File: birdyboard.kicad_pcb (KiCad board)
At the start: 2 copper layers, 18 parts, among them J1 24V Input Screw Terminal, J10 JST-PH StepMotor Conn, J11 TBP02R2-381-04BE, J2 24V Input Screw Terminal, J3 24V Input Screw Terminal, J4 JST-PH StepMotor Conn, J5 JST-PH StepMotor Conn, J6 JST-PH StepMotor Conn, J7 TBP02R2-381-04BE, J8 TBP02R2-381-04BE, J9 TBP02R2-381-04BE, U1 TMC2208_SILENTSTEPSTICK, U2 TMC2208_SILENTSTEPSTICK, U3 Pico, U4 TMC2208_SILENTSTEPSTICK, U5 TMC2208_SILENTSTEPSTICK, U7 AZ1117CH-3_3TRG1

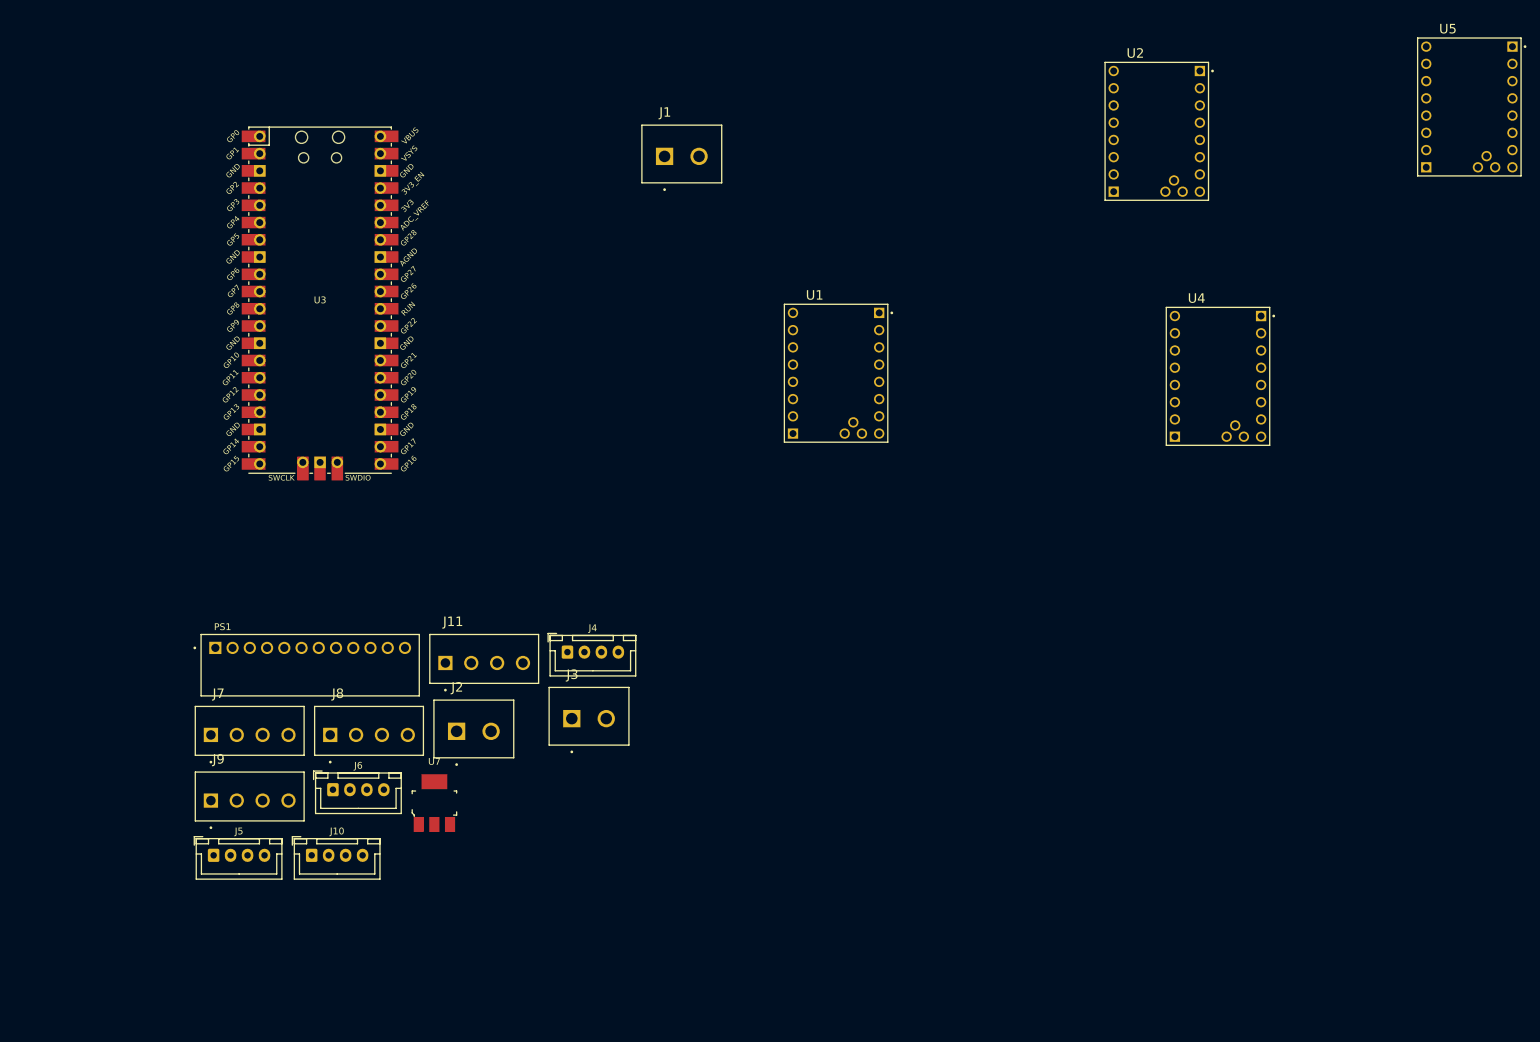
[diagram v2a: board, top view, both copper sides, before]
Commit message: Fixes most footprints and places footprints roughly at their final resting place
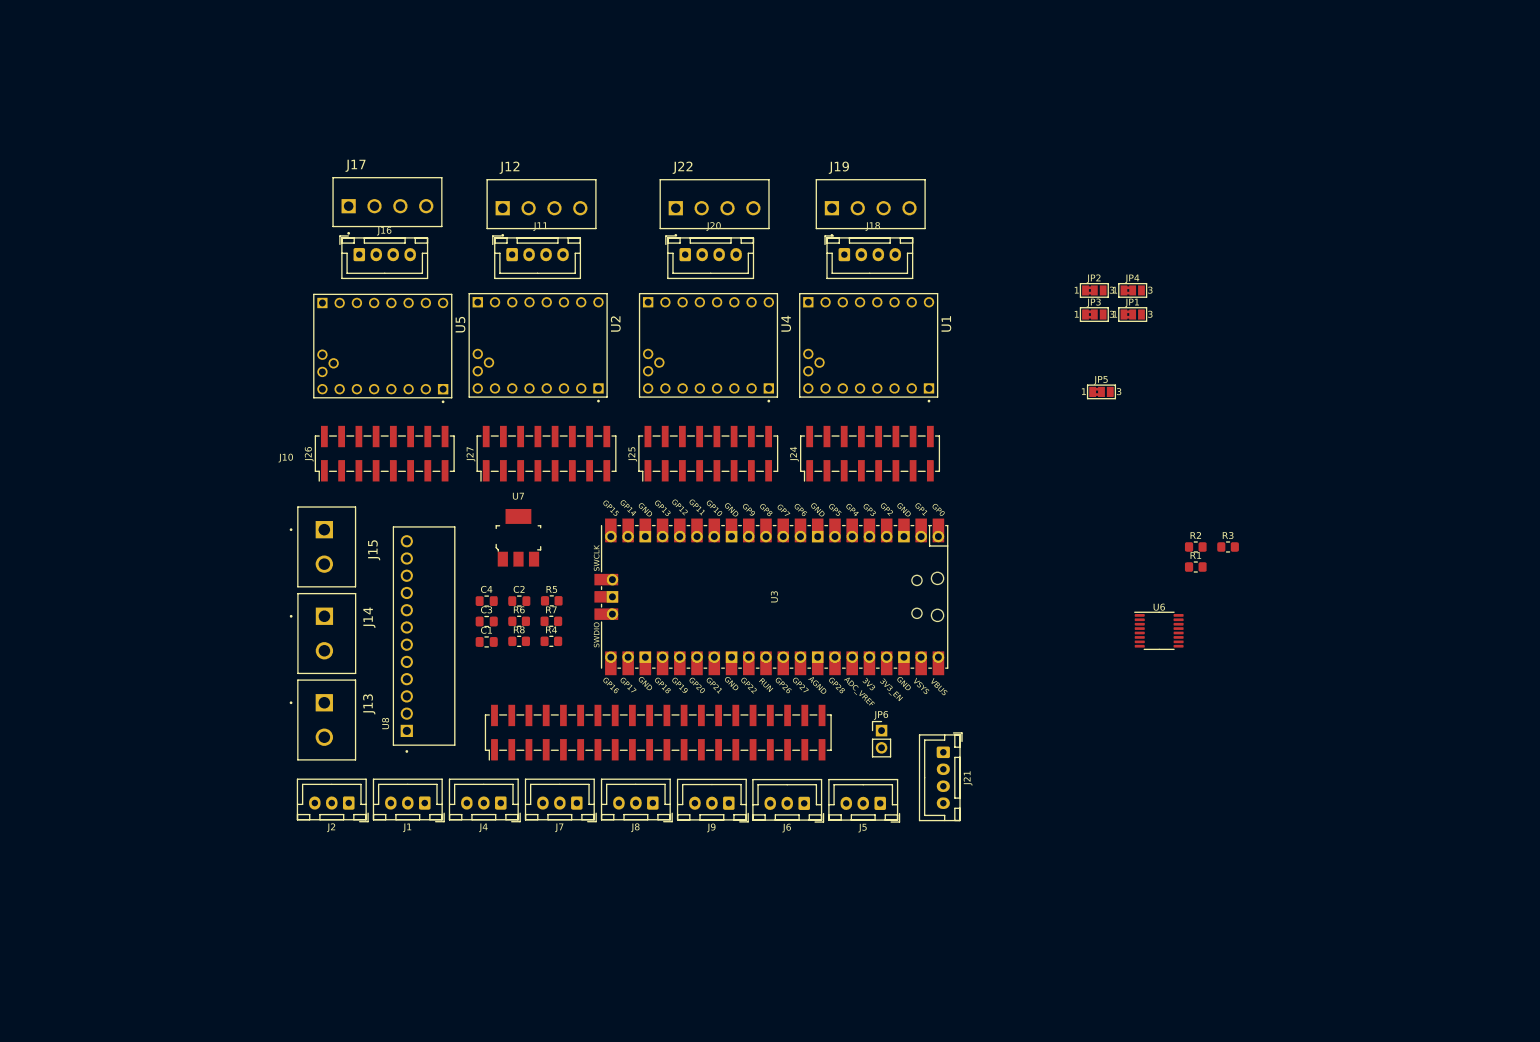
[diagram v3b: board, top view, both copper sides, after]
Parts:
- removed J3: 24V Input Screw Terminal, birdyboard:CUI_TBP01R2-508-02BE
- removed PS1: K7805-3AR3, birdyboard:CONV_K7805-3AR3
- added C1: 10uF 50V, Capacitor_SMD:C_0805_2012Metric_Pad1.18x1.45mm_HandSolder, F.Cu at (101.3, 118.4)
- added C2: 10uF 10V, Capacitor_SMD:C_0805_2012Metric_Pad1.18x1.45mm_HandSolder, F.Cu at (106.1, 112.4)
- added C3: 22uF 10V, Capacitor_SMD:C_0805_2012Metric_Pad1.18x1.45mm_HandSolder, F.Cu at (101.3, 115.4)
- added C4: 22uF 10V, Capacitor_SMD:C_0805_2012Metric_Pad1.18x1.45mm_HandSolder, F.Cu at (101.3, 112.4)
- added J12: TBP02R2-381-04BE, birdyboard:CUI_TBP02R2-381-04BE, F.Cu at (103.7, 54.5)
- added J13: Screw_Terminal_01x02, birdyboard:CUI_TBP01R2-508-02BE, F.Cu at (77.4, 127.4)
- added J14: Screw_Terminal_01x02, birdyboard:CUI_TBP01R2-508-02BE, F.Cu at (77.4, 114.7)
- added J15: Screw_Terminal_01x02, birdyboard:CUI_TBP01R2-508-02BE, F.Cu at (77.4, 101.9)
- added J16: JST-PH StepMotor Conn, Connector_JST:JST_XH_B4B-XH-A_1x04_P2.50mm_Vertical, F.Cu at (82.5, 61.4)
- added J17: TBP02R2-381-04BE, birdyboard:CUI_TBP02R2-381-04BE, F.Cu at (81.0, 54.2)
- added J18: JST-PH StepMotor Conn, Connector_JST:JST_XH_B4B-XH-A_1x04_P2.50mm_Vertical, F.Cu at (154.0, 61.4)
- added J19: TBP02R2-381-04BE, birdyboard:CUI_TBP02R2-381-04BE, F.Cu at (152.2, 54.5)
- added J20: JST-PH StepMotor Conn, Connector_JST:JST_XH_B4B-XH-A_1x04_P2.50mm_Vertical, F.Cu at (130.6, 61.4)
- added J21: JST-PH UART Conn, Connector_JST:JST_XH_B4B-XH-A_1x04_P2.50mm_Vertical, F.Cu at (168.6, 134.7)
- added J22: TBP02R2-381-04BE, birdyboard:CUI_TBP02R2-381-04BE, F.Cu at (129.2, 54.5)
- added J24: AS5047_Adapter_Board_Connector, Connector_PinHeader_2.54mm:PinHeader_2x08_P2.54mm_Vertical_SMD, F.Cu at (157.8, 90.7)
- added J25: AS5047_Adapter_Board_Connector, Connector_PinHeader_2.54mm:PinHeader_2x08_P2.54mm_Vertical_SMD, F.Cu at (134.0, 90.7)
- added J26: AS5047_Adapter_Board_Connector, Connector_PinHeader_2.54mm:PinHeader_2x08_P2.54mm_Vertical_SMD, F.Cu at (86.3, 90.7)
- added J27: AS5047_Adapter_Board_Connector, Connector_PinHeader_2.54mm:PinHeader_2x08_P2.54mm_Vertical_SMD, F.Cu at (110.1, 90.7)
- added JP1: SolderJumper_3_Bridged12, Jumper:SolderJumper-3_P1.3mm_Bridged2Bar12_Pad1.0x1.5mm_NumberLabels, F.Cu at (196.5, 70.2)
- added JP2: SolderJumper_3_Bridged12, Jumper:SolderJumper-3_P1.3mm_Bridged2Bar12_Pad1.0x1.5mm_NumberLabels, F.Cu at (190.8, 66.7)
- added JP3: SolderJumper_3_Bridged12, Jumper:SolderJumper-3_P1.3mm_Bridged2Bar12_Pad1.0x1.5mm_NumberLabels, F.Cu at (190.8, 70.2)
- added JP4: SolderJumper_3_Bridged12, Jumper:SolderJumper-3_P1.3mm_Bridged2Bar12_Pad1.0x1.5mm_NumberLabels, F.Cu at (196.5, 66.7)
- added JP5: Jumper_3_Open, Jumper:SolderJumper-3_P1.3mm_Bridged2Bar12_Pad1.0x1.5mm_NumberLabels, F.Cu at (191.9, 81.6)
- added JP6: Jumper_2_Open, Connector_PinHeader_2.54mm:PinHeader_1x02_P2.54mm_Vertical, F.Cu at (159.5, 131.5)
- added R1: R, Resistor_SMD:R_0805_2012Metric_Pad1.20x1.40mm_HandSolder, F.Cu at (205.8, 107.4)
- added R2: R, Resistor_SMD:R_0805_2012Metric_Pad1.20x1.40mm_HandSolder, F.Cu at (205.8, 104.5)
- added R3: R, Resistor_SMD:R_0805_2012Metric_Pad1.20x1.40mm_HandSolder, F.Cu at (210.6, 104.5)
- added R4: R, Resistor_SMD:R_0805_2012Metric_Pad1.20x1.40mm_HandSolder, F.Cu at (110.8, 118.3)
- added R5: R, Resistor_SMD:R_0805_2012Metric_Pad1.20x1.40mm_HandSolder, F.Cu at (110.9, 112.4)
- added R6: R, Resistor_SMD:R_0805_2012Metric_Pad1.20x1.40mm_HandSolder, F.Cu at (106.1, 115.4)
- added R7: R, Resistor_SMD:R_0805_2012Metric_Pad1.20x1.40mm_HandSolder, F.Cu at (110.8, 115.4)
- added R8: R, Resistor_SMD:R_0805_2012Metric_Pad1.20x1.40mm_HandSolder, F.Cu at (106.1, 118.3)
- added U6: SN74CBT3253 MUX/DEMUX, Package_SO:TSSOP-16_4.4x5mm_P0.65mm, F.Cu at (200.4, 116.8)
- added U8: K7805-3AR3, birdyboard:CONV_K7805-3AR3, F.Cu at (92.1, 117.6)
- J1, J2: value 24V Input Screw Terminal -> JST_3pin; footprint birdyboard:CUI_TBP01R2-508-02BE -> Connector_JST:JST_XH_B3B-XH-A_1x03_P2.50mm_Vertical
- J10: value JST-PH StepMotor Conn -> Conn_02x20_Odd_Even; footprint Connector_JST:JST_XH_B4B-XH-A_1x04_P2.50mm_Vertical -> Connector_PinHeader_2.54mm:PinHeader_2x20_P2.54mm_Vertical_SMD
- J11: value TBP02R2-381-04BE -> JST-PH StepMotor Conn; footprint birdyboard:CUI_TBP02R2-381-04BE -> Connector_JST:JST_XH_B4B-XH-A_1x04_P2.50mm_Vertical
- J4, J5, J6: value JST-PH StepMotor Conn -> JST_3pin; footprint Connector_JST:JST_XH_B4B-XH-A_1x04_P2.50mm_Vertical -> Connector_JST:JST_XH_B3B-XH-A_1x03_P2.50mm_Vertical
- J7, J8, J9: value TBP02R2-381-04BE -> JST_3pin; footprint birdyboard:CUI_TBP02R2-381-04BE -> Connector_JST:JST_XH_B3B-XH-A_1x03_P2.50mm_Vertical
- U1, U2, U4, U5: value TMC2208_SILENTSTEPSTICK -> TMC2209_SILENTSTEPSTICK
- moved U5 163.9 mm to (86.0, 74.8), turned to -90 degrees
- moved J1 101.6 mm to (92.2, 142.2), turned to 180 degrees
- moved J5 98.5 mm to (159.3, 142.2), turned to 180 degrees
- moved U2 96.5 mm to (108.9, 74.7), turned to -90 degrees
- moved U3 80.0 mm to (143.7, 111.8), turned to -90 degrees
- moved J9 76.3 mm to (137.0, 142.2), turned to 180 degrees
- moved U4 75.2 mm to (134.0, 74.7), turned to -90 degrees
- moved J6 69.5 mm to (148.1, 142.2), turned to 180 degrees
- moved J11 61.0 mm to (105.1, 61.4)
- moved J7 54.8 mm to (114.6, 142.2), turned to 180 degrees
- moved J10 54.2 mm to (126.6, 131.8), turned to 90 degrees
- moved J8 48.6 mm to (125.8, 142.2), turned to 180 degrees
- moved U7 41.0 mm to (106.0, 103.1)
- moved J4 24.3 mm to (103.4, 142.2), turned to 180 degrees
- moved J2 19.1 mm to (81.0, 142.2), turned to 180 degrees
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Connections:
- J1 pad 1: (no net) -> +3V3
- J1 pad 2: (no net) -> GPIO17
- J10 pad 1: Net-(J10-Pad1) -> +3.3V
- J10 pad 2: Net-(J10-Pad2) -> +5V
- J10 pad 3: Net-(J10-Pad3) -> unconnected-(J10-Pad3)
- J10 pad 4: Net-(J10-Pad4) -> PICO_VBus
- J11 pad 1: unconnected-(J11-Pad1) -> Motor1A1
- J11 pad 2: unconnected-(J11-Pad2) -> Motor1A2
- J11 pad 3: unconnected-(J11-Pad3) -> Motor1B1
- J11 pad 4: unconnected-(J11-Pad4) -> Motor1B2
- J2 pad 1: (no net) -> +3V3
- J2 pad 2: (no net) -> GPIO16
- J4 pad 1: Net-(J4-Pad1) -> +3V3
- J4 pad 2: Net-(J4-Pad2) -> GPIO18
- J4 pad 3: Net-(J4-Pad3) -> GND
- J5 pad 1: Net-(J5-Pad1) -> +3V3
- J5 pad 2: Net-(J5-Pad2) -> GPIO26
- J5 pad 3: Net-(J5-Pad3) -> GND
- J6 pad 1: Net-(J6-Pad1) -> +3V3
- J6 pad 2: Net-(J6-Pad2) -> GPIO27
- J6 pad 3: Net-(J6-Pad3) -> GND
- J7 pad 1: unconnected-(J7-Pad1) -> +3V3
- J7 pad 2: unconnected-(J7-Pad2) -> GPIO19
- J7 pad 3: unconnected-(J7-Pad3) -> GND
- J8 pad 1: unconnected-(J8-Pad1) -> +3V3
- J8 pad 2: unconnected-(J8-Pad2) -> GPIO20
- J8 pad 3: unconnected-(J8-Pad3) -> GND
- J9 pad 1: unconnected-(J9-Pad1) -> +3V3
- J9 pad 2: unconnected-(J9-Pad2) -> GPIO21
- J9 pad 3: unconnected-(J9-Pad3) -> GND
- U1 pad JP1_3: (no net) -> Net-(JP1-Pad1)
- U1 pad JP1_4: unconnected-(U1-PadJP1_4) -> Net-(JP1-Pad3)
- U1 pad JP1_6: unconnected-(U1-PadJP1_6) -> GND
- U1 pad JP1_7: unconnected-(U1-PadJP1_7) -> GND
- U1 pad JP1_8: unconnected-(U1-PadJP1_8) -> Net-(R4-Pad2)
- U1 pad JP2_3: Net-(J4-Pad2) -> Motor3A2
- U1 pad JP2_4: Net-(J4-Pad1) -> Motor3A1
- U1 pad JP2_5: Net-(J4-Pad3) -> Motor3B1
- U1 pad JP2_6: Net-(J4-Pad4) -> Motor3B2
- U1 pad JP2_7: unconnected-(U1-PadJP2_7) -> +3V3
- U2 pad JP1_3: (no net) -> Net-(JP2-Pad1)
- U2 pad JP1_4: unconnected-(U2-PadJP1_4) -> Net-(JP2-Pad3)
- U2 pad JP1_6: unconnected-(U2-PadJP1_6) -> +3V3
- U2 pad JP1_7: unconnected-(U2-PadJP1_7) -> GND
- U2 pad JP1_8: unconnected-(U2-PadJP1_8) -> Net-(R5-Pad2)
- U2 pad JP2_3: Net-(J5-Pad2) -> Motor1A2
- U2 pad JP2_4: Net-(J5-Pad1) -> Motor1A1
- U2 pad JP2_5: Net-(J5-Pad3) -> Motor1B1
- U2 pad JP2_6: Net-(J5-Pad4) -> Motor1B2
- U2 pad JP2_7: unconnected-(U2-PadJP2_7) -> +3V3
- U3 pad 1: unconnected-(U3-Pad1) -> GPIO0
- U3 pad 11: unconnected-(U3-Pad11) -> SPIMux_S0
- U3 pad 12: unconnected-(U3-Pad12) -> SPI_CSn
- U3 pad 14: unconnected-(U3-Pad14) -> SPI_SCK
- U3 pad 15: unconnected-(U3-Pad15) -> SPI_MOSI
- U3 pad 16: unconnected-(U3-Pad16) -> SPI_MISO
- U3 pad 17: unconnected-(U3-Pad17) -> SPIMux_S1
- U3 pad 2: unconnected-(U3-Pad2) -> TMC_UART
- U3 pad 21: unconnected-(U3-Pad21) -> GPIO16
- U3 pad 22: unconnected-(U3-Pad22) -> GPIO17
- U3 pad 24: unconnected-(U3-Pad24) -> GPIO18
- U3 pad 25: unconnected-(U3-Pad25) -> GPIO19
- U3 pad 26: unconnected-(U3-Pad26) -> GPIO20
- U3 pad 27: unconnected-(U3-Pad27) -> GPIO21
- U3 pad 31: unconnected-(U3-Pad31) -> GPIO27
- U3 pad 32: unconnected-(U3-Pad32) -> GPIO26
- U3 pad 36: unconnected-(U3-Pad36) -> PICO_3V3
- U3 pad 38: unconnected-(U3-Pad38) -> GND
- U3 pad 39: unconnected-(U3-Pad39) -> PICO_VSys
- U3 pad 40: unconnected-(U3-Pad40) -> PICO_VBus
- U3 pad 6: unconnected-(U3-Pad6) -> UART_TX
- U3 pad 7: unconnected-(U3-Pad7) -> UART_RX
- U4 pad JP1_3: (no net) -> Net-(JP3-Pad1)
- U4 pad JP1_4: unconnected-(U4-PadJP1_4) -> Net-(JP3-Pad3)
- U4 pad JP1_6: unconnected-(U4-PadJP1_6) -> GND
- U4 pad JP1_7: unconnected-(U4-PadJP1_7) -> +3V3
- U4 pad JP1_8: unconnected-(U4-PadJP1_8) -> Net-(R7-Pad2)
- U4 pad JP2_3: Net-(J6-Pad2) -> Motor4A2
- U4 pad JP2_4: Net-(J6-Pad1) -> Motor4A1
- U4 pad JP2_5: Net-(J6-Pad3) -> Motor4B1
- U4 pad JP2_6: Net-(J6-Pad4) -> Motor4B2
- U4 pad JP2_7: unconnected-(U4-PadJP2_7) -> +3V3
- U5 pad JP1_3: (no net) -> Net-(JP4-Pad1)
- U5 pad JP1_4: unconnected-(U5-PadJP1_4) -> Net-(JP4-Pad3)
- U5 pad JP1_6: unconnected-(U5-PadJP1_6) -> +3V3
- U5 pad JP1_7: unconnected-(U5-PadJP1_7) -> +3V3
- U5 pad JP1_8: unconnected-(U5-PadJP1_8) -> Net-(R8-Pad2)
- U5 pad JP2_3: Net-(J10-Pad2) -> Motor2A2
- U5 pad JP2_4: Net-(J10-Pad1) -> Motor2A1
- U5 pad JP2_5: Net-(J10-Pad3) -> Motor2B1
- U5 pad JP2_6: Net-(J10-Pad4) -> Motor2B2
- U5 pad JP2_7: unconnected-(U5-PadJP2_7) -> +3V3
- U7 pad 1: unconnected-(U7-Pad1) -> GND
- U7 pad 2: unconnected-(U7-Pad2) -> +3.3V
- U7 pad 3: unconnected-(U7-Pad3) -> +5V
- U7 pad 4: unconnected-(U7-Pad4) -> +3.3V

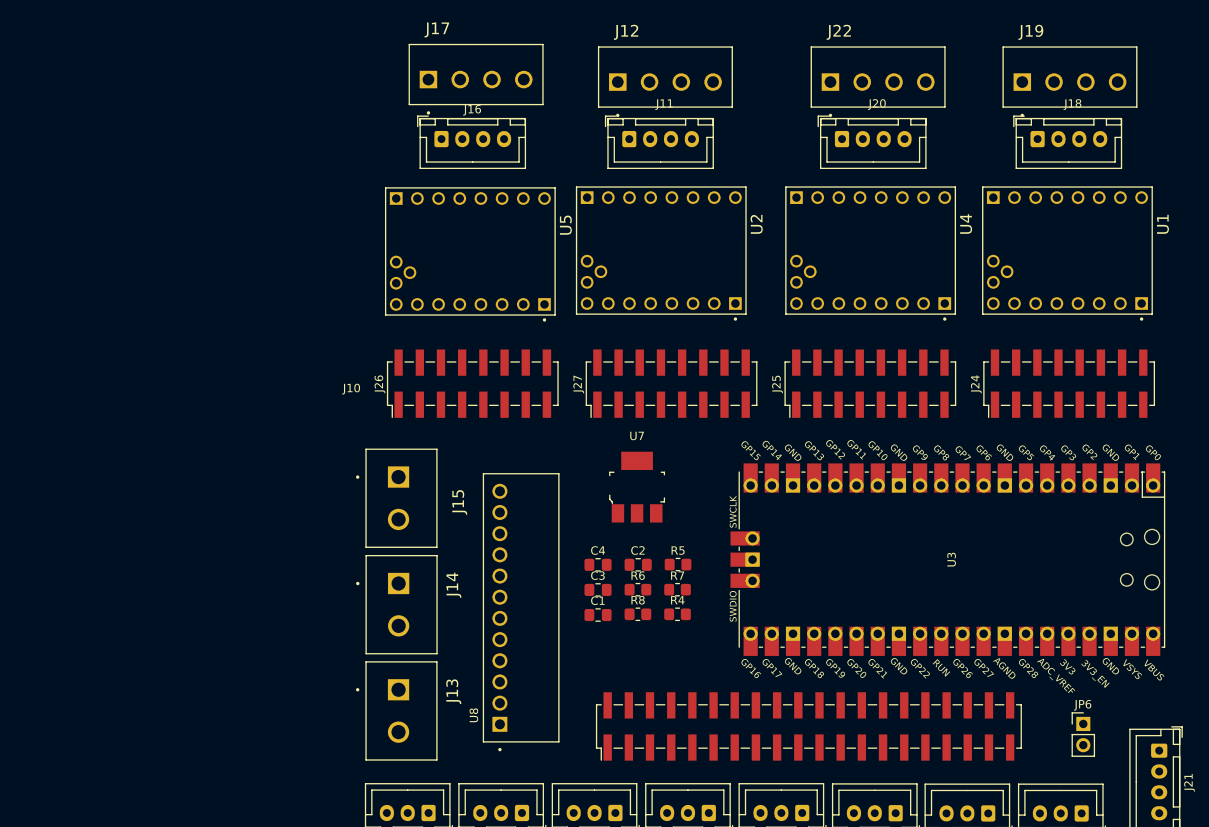
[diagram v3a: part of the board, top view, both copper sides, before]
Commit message: -- Adds copper pours -- Adds netclasses & constraints for each netclasses -- Adds some pcb routes for some connections
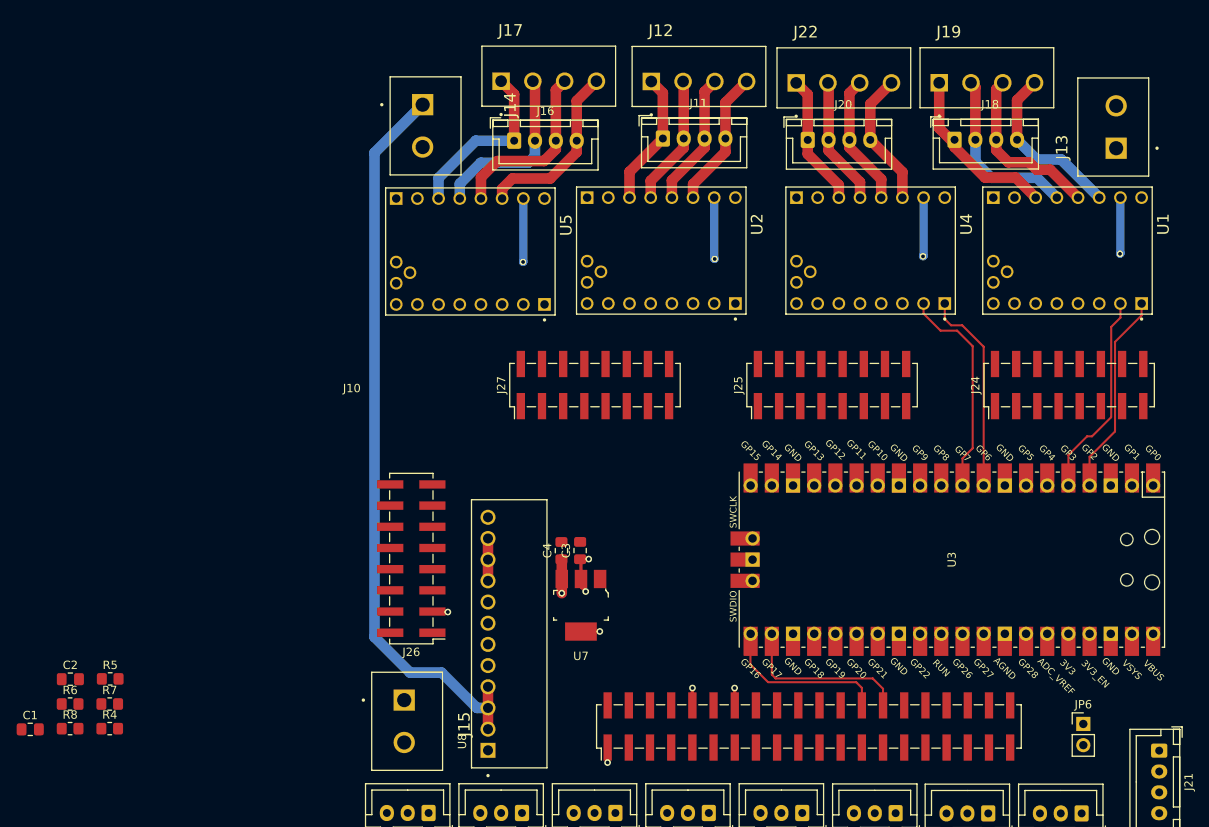
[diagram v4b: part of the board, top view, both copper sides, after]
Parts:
- moved J13 107.8 mm to (163.4, 62.5), turned to 90 degrees
- moved C2 69.4 mm to (38.0, 126.1)
- moved R5 69.4 mm to (42.8, 126.1)
- moved C1 69.4 mm to (33.2, 132.2)
- moved R4 69.4 mm to (42.8, 132.1)
- moved R6 69.4 mm to (38.0, 129.1)
- moved R7 69.4 mm to (42.8, 129.1)
- moved R8 69.4 mm to (38.0, 132.1)
- moved J14 57.5 mm to (80.3, 57.2)
- moved J15 26.7 mm to (78.1, 128.6)
- moved J26 22.2 mm to (78.9, 111.7), turned to 180 degrees
- moved U7 15.7 mm to (99.3, 117.3), turned to 180 degrees
- moved J18 9.96 mm to (144.1, 61.5)
- moved J19 9.96 mm to (142.2, 54.6)
- moved J27 9.18 mm to (101.0, 90.9)
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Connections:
- J1 pad 1: +3V3 -> +3.3V
- J10 pad 11: unconnected-(J10-Pad11) -> DIR_1
- J10 pad 13: unconnected-(J10-Pad13) -> SPIMux_S1
- J10 pad 15: unconnected-(J10-Pad15) -> SPI_MISO
- J10 pad 19: unconnected-(J10-Pad19) -> SPI_MOSI
- J10 pad 21: unconnected-(J10-Pad21) -> SPI_SCK
- J10 pad 23: unconnected-(J10-Pad23) -> SPI_CSn
- J10 pad 25: unconnected-(J10-Pad25) -> SPIMux_S0
- J10 pad 26: GPIO21 -> GPIO16
- J10 pad 27: unconnected-(J10-Pad27) -> STEP_0
- J10 pad 28: GPIO20 -> GPIO17
- J10 pad 29: unconnected-(J10-Pad29) -> DIR_0
- J10 pad 3: unconnected-(J10-Pad3) -> GPIO0
- J10 pad 30: GPIO19 -> GPIO18
- J10 pad 31: unconnected-(J10-Pad31) -> UART_RX
- J10 pad 32: GPIO18 -> GPIO19
- J10 pad 33: unconnected-(J10-Pad33) -> UART_TX
- J10 pad 36: GPIO17 -> GPIO20
- J10 pad 37: unconnected-(J10-Pad37) -> STEP_3
- J10 pad 38: GPIO16 -> GPIO21
- J10 pad 39: GND -> DIR_3
- J10 pad 9: unconnected-(J10-Pad9) -> STEP_1
- J2 pad 1: +3V3 -> +3.3V
- J24 pad 3: +3V3 -> +3.3V
- J4 pad 1: +3V3 -> +3.3V
- J5 pad 1: +3V3 -> +3.3V
- J6 pad 1: +3V3 -> +3.3V
- J7 pad 1: +3V3 -> +3.3V
- J8 pad 1: +3V3 -> +3.3V
- J9 pad 1: +3V3 -> +3.3V
- R1 pad 1: +3V3 -> +3.3V
- R2 pad 1: +3V3 -> +3.3V
- R3 pad 1: +3V3 -> +3.3V
- R4 pad 1: +3V3 -> +3.3V
- R5 pad 1: +3V3 -> +3.3V
- R7 pad 1: +3V3 -> +3.3V
- R8 pad 1: +3V3 -> +3.3V
- U1 pad JP2_3: Motor3A2 -> Motor3A1
- U1 pad JP2_4: Motor3A1 -> Motor3A2
- U1 pad JP2_7: +3V3 -> +3.3V
- U2 pad JP1_6: +3V3 -> +3.3V
- U2 pad JP2_3: Motor1A2 -> Motor1A1
- U2 pad JP2_4: Motor1A1 -> Motor1A2
- U2 pad JP2_7: +3V3 -> +3.3V
- U3 pad 29: DIR_2 -> STEP_2
- U3 pad 31: GPIO27 -> GPIO26
- U3 pad 32: GPIO26 -> GPIO27
- U3 pad 34: STEP_2 -> DIR_2
- U4 pad JP1_7: +3V3 -> +3.3V
- U4 pad JP2_3: Motor4A2 -> Motor4A1
- U4 pad JP2_4: Motor4A1 -> Motor4A2
- U4 pad JP2_7: +3V3 -> +3.3V
- U5 pad JP1_6: +3V3 -> +3.3V
- U5 pad JP1_7: +3V3 -> +3.3V
- U5 pad JP2_3: Motor2A2 -> Motor2A1
- U5 pad JP2_4: Motor2A1 -> Motor2A2
- U5 pad JP2_7: +3V3 -> +3.3V
- U6 pad 16: +3V3 -> +3.3V
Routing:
- net +24V: track 0.00 -> 88.4 mm
- net +3.3V: track 0.00 -> 44.2 mm, vias 0 -> 11
- net STEP_0: track 0.00 -> 25.9 mm
- net STEP_3: track 0.00 -> 24.7 mm
- net DIR_0: track 0.00 -> 24.5 mm
- net DIR_3: track 0.00 -> 24.4 mm
- net Motor3A2: track 0.00 -> 21.5 mm
- net Motor2B1: track 0.00 -> 21.5 mm
- net Motor2B2: track 0.00 -> 21.4 mm
- net Motor2A2: track 0.00 -> 21.2 mm
- net Motor3A1: track 0.00 -> 21.2 mm
- net Motor2A1: track 0.00 -> 21.2 mm
- net GPIO17: track 0.00 -> 20.9 mm
- net Motor3B1: track 0.00 -> 20.8 mm
- net Motor3B2: track 0.00 -> 20.6 mm
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- added copper zone on In1.Cu, net +24V
- added copper zone on In1.Cu, net +3.3V
- added copper zone on In1.Cu, net +5V
- added copper zone on In2.Cu, net GND
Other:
- copper layers 2 -> 4

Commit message: lay out some routes - place last components
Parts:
- JP1, JP2, JP3, JP4: moved to B.Cu
- moved R6 132.2 mm to (166.6, 98.5)
- moved R4 117.3 mm to (149.6, 83.6)
- moved JP4 108.7 mm to (88.6, 79.9), turned to 180 degrees
- moved R7 93.8 mm to (125.1, 84.1)
- moved C1 93.7 mm to (81.3, 51.7)
- moved U6 92.1 mm to (108.9, 106.2)
- moved JP5 85.3 mm to (108.7, 100.3)
- moved R3 85.2 mm to (127.8, 124.6)
- moved JP2 80.4 mm to (111.5, 79.8), turned to 180 degrees
- moved R2 76.2 mm to (132.3, 124.6)
- moved R1 71.3 mm to (136.6, 124.7), turned to 180 degrees
- moved R5 70.4 mm to (100.1, 85.1)
- moved R8 62.3 mm to (78.2, 84.4)
- moved JP3 55.1 mm to (136.6, 79.7), turned to 180 degrees
- moved C2 46.9 mm to (84.6, 131.9), turned to -90 degrees
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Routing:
- net TMC_UART: track 0.00 -> 103.4 mm, vias 0 -> 4
- net DIR_2: track 0.00 -> 85.2 mm
- net ENC_CS_4: track 0.00 -> 81.0 mm, vias 0 -> 2
- net STEP_2: track 0.00 -> 74.5 mm
- net UART_RX: track 0.00 -> 50.9 mm
- net UART_TX: track 0.00 -> 45.6 mm
- net ENC_CS_1: track 0.00 -> 29.2 mm, vias 0 -> 2
- net GND: track 0.00 -> 24.8 mm, vias 0 -> 4
- net STEP_1: track 0.00 -> 23.6 mm
- net DIR_1: track 0.00 -> 23.6 mm
- net ENC_CS_2: track 0.00 -> 15.5 mm
- net SPI_CS: track 0.00 -> 9.57 mm
- net ENC_CS_1_Muxed: track 0.00 -> 8.62 mm
- net +5V: track 9.16 -> 16.6 mm
- net ENC_CS_3: track 0.00 -> 6.00 mm
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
